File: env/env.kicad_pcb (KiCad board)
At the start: 2 copper layers, 69.1 x 99.6 mm, 35 parts, among them J1 Conn_01x02_Socket, J2 Conn_01x03_Socket, J3 Conn_01x02_Socket, J4 Conn_01x02_Socket, Q1 BC548C, SW1 SW_SPDT, U1 TL074, U2 TL074

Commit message: turn vca to dual vca add mounting holes
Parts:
- added H1: MountingHole, MountingHole:MountingHole_2.1mm, F.Cu at (166.1, 51.3)
- added H2: MountingHole, MountingHole:MountingHole_2.1mm, F.Cu at (107.7, 50.8)
- added H3: MountingHole, MountingHole:MountingHole_2.1mm, F.Cu at (164.1, 137.7)
- added H4: MountingHole, MountingHole:MountingHole_2.1mm, F.Cu at (110.2, 137.7)
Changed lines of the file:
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@@
   (net 28 "Net-(U2C--)")
   (net 29 "Net-(U2D--)")
+  (footprint "MountingHole:MountingHole_2.1mm" (layer "F.Cu")
+    (at 164.084 137.668)
+    (descr "Mounting Hole 2.1mm, no annular")
+    (tags "mounting hole 2.1mm no annular")
+    (property "Sheetfile" "env.kicad_sch")
+    (property "Sheetname" "")
+    (property "ki_description" "Mounting Hole without connection")
+    (property "ki_keywords" "mounting hole")
+    (attr exclude_from_pos_files)
+    (fp_text reference "H3" (at 0 -3.2) (layer "F.SilkS")
+        (effects (font (size 1 1) (thickness 0.15)))
+    )
+    (fp_text value "MountingHole" (at 0 3.2) (layer "F.Fab")
+        (effects (font (size 1 1) (thickness 0.15)))
+    )
+    (fp_text user "${REFERENCE}" (at 0 0) (layer "F.Fab")
+        (effects (font (size 1 1) (thickness 0.15)))
+    )
+    (fp_circle (center 0 0) (end 2.1 0)
+      (stroke (width 0.15) (type solid)) (fill none) (layer "Cmts.User"))
+    (fp_circle (center 0 0) (end 2.35 0)
+      (stroke (width 0.05) (type solid)) (fill none) (layer "F.CrtYd"))
+    (pad "" np_thru_hole circle (at 0 0) (size 2.1 2.1) (drill 2.1) (layers "*.Cu" "*.Mask"))
+  )
   (footprint "my_library:my_dip14" (layer "F.Cu")
     (at 132.1598 64.516)
@@
     )
   )
+  (footprint "MountingHole:MountingHole_2.1mm" (layer "F.Cu")
+    (at 110.236 137.668)
+    (descr "Mounting Hole 2.1mm, no annular")
+    (tags "mounting hole 2.1mm no annular")
+    (property "Sheetfile" "env.kicad_sch")
+    (property "Sheetname" "")
+    (property "ki_description" "Mounting Hole without connection")
+    (property "ki_keywords" "mounting hole")
+    (attr exclude_from_pos_files)
+    (fp_text reference "H4" (at 0 -3.2) (layer "F.SilkS")
+        (effects (font (size 1 1) (thickness 0.15)))
+    )
+    (fp_text value "MountingHole" (at 0 3.2) (layer "F.Fab")
+        (effects (font (size 1 1) (thickness 0.15)))
+    )
+    (fp_text user "${REFERENCE}" (at 0 0) (layer "F.Fab")
+        (effects (font (size 1 1) (thickness 0.15)))
+    )
+    (fp_circle (center 0 0) (end 2.1 0)
+      (stroke (width 0.15) (type solid)) (fill none) (layer "Cmts.User"))
+    (fp_circle (center 0 0) (end 2.35 0)
+      (stroke (width 0.05) (type solid)) (fill none) (layer "F.CrtYd"))
+    (pad "" np_thru_hole circle (at 0 0) (size 2.1 2.1) (drill 2.1) (layers "*.Cu" "*.Mask"))
+  )
   (footprint "my_library:my_really_cool_2pin" (layer "F.Cu")
     (at 161.1108 104.648)
@@
     (pad "3" thru_hole circle (at 0 7.62) (size 2.54 2.54) (drill 1) (layers "*.Cu" "*.Mask")
       (net 2 "GND") (pinfunction "3") (pintype "passive"))
+  )
+  (footprint "MountingHole:MountingHole_2.1mm" (layer "F.Cu")
+    (at 166.116 51.308)
+    (descr "Mounting Hole 2.1mm, no annular")
+    (tags "mounting hole 2.1mm no annular")
+    (property "Sheetfile" "env.kicad_sch")
+    (property "Sheetname" "")
+    (property "ki_description" "Mounting Hole without connection")
+    (property "ki_keywords" "mounting hole")
+    (attr exclude_from_pos_files)
+    (fp_text reference "H1" (at 0 -3.2) (layer "F.SilkS")
+        (effects (font (size 1 1) (thickness 0.15)))
+    )
+    (fp_text value "MountingHole" (at 0 3.2) (layer "F.Fab")
+        (effects (font (size 1 1) (thickness 0.15)))
+    )
+    (fp_text user "${REFERENCE}" (at 0 0) (layer "F.Fab")
+        (effects (font (size 1 1) (thickness 0.15)))
+    )
+    (fp_circle (center 0 0) (end 2.1 0)
+      (stroke (width 0.15) (type solid)) (fill none) (layer "Cmts.User"))
+    (fp_circle (center 0 0) (end 2.35 0)
+      (stroke (width 0.05) (type solid)) (fill none) (layer "F.CrtYd"))
+    (pad "" np_thru_hole circle (at 0 0) (size 2.1 2.1) (drill 2.1) (layers "*.Cu" "*.Mask"))
   )
   (footprint "my_library:my_really_cool_3pin" (layer "F.Cu")
@@
       (net 14 "Net-(D7-A)") (pintype "passive") (solder_mask_margin 0.102))
   )
+  (footprint "MountingHole:MountingHole_2.1mm" (layer "F.Cu")
+    (at 107.696 50.8)
+    (descr "Mounting Hole 2.1mm, no annular")
+    (tags "mounting hole 2.1mm no annular")
+    (property "Sheetfile" "env.kicad_sch")
+    (property "Sheetname" "")
+    (property "ki_description" "Mounting Hole without connection")
+    (property "ki_keywords" "mounting hole")
+    (attr exclude_from_pos_files)
+    (fp_text reference "H2" (at 0 -3.2) (layer "F.SilkS")
+        (effects (font (size 1 1) (thickness 0.15)))
+    )
+    (fp_text value "MountingHole" (at 0 3.2) (layer "F.Fab")
+        (effects (font (size 1 1) (thickness 0.15)))
+    )
+    (fp_text user "${REFERENCE}" (at 0 0) (layer "F.Fab")
+        (effects (font (size 1 1) (thickness 0.15)))
+    )
+    (fp_circle (center 0 0) (end 2.1 0)
+      (stroke (width 0.15) (type solid)) (fill none) (layer "Cmts.User"))
+    (fp_circle (center 0 0) (end 2.35 0)
+      (stroke (width 0.05) (type solid)) (fill none) (layer "F.CrtYd"))
+    (pad "" np_thru_hole circle (at 0 0) (size 2.1 2.1) (drill 2.1) (layers "*.Cu" "*.Mask"))
+  )
   (footprint "Resistor_THT:R_Axial_DIN0204_L3.6mm_D1.6mm_P7.62mm_Horizontal" (layer "F.Cu")

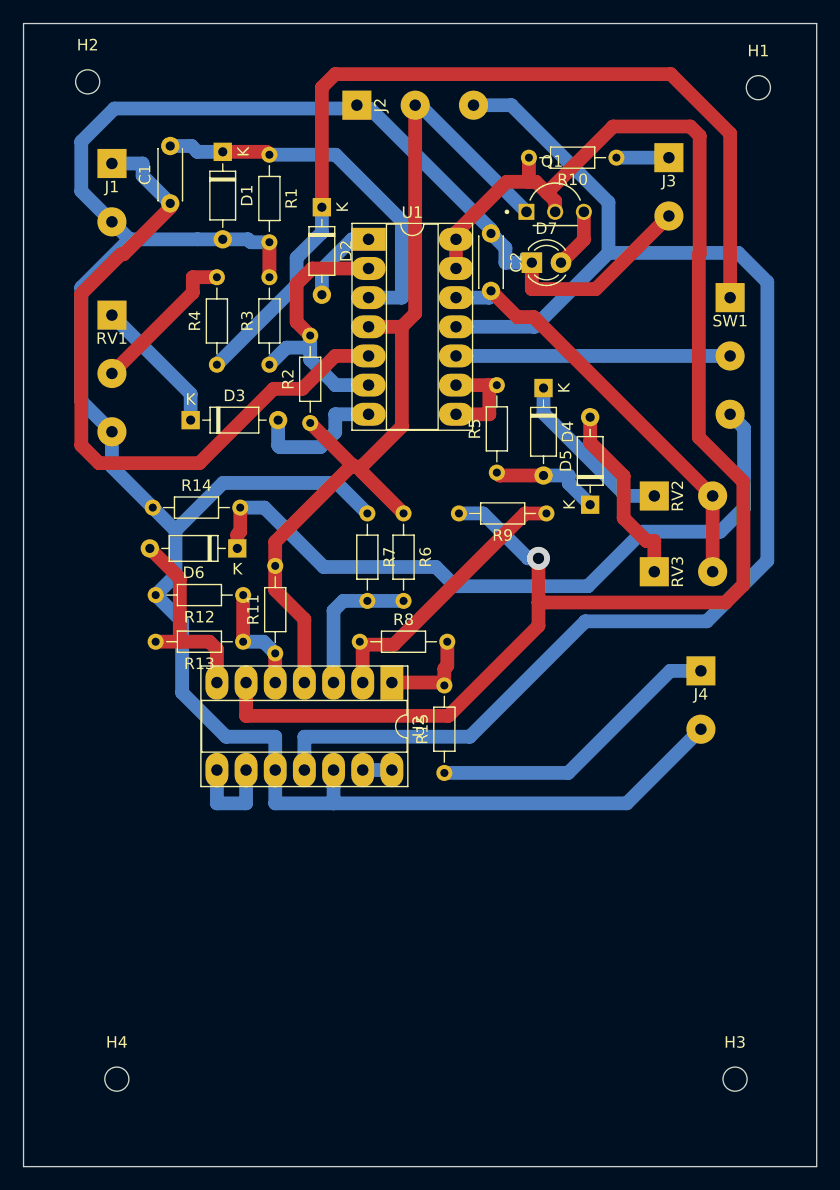
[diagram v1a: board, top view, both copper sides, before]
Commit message: use custom footprints with bigger pads
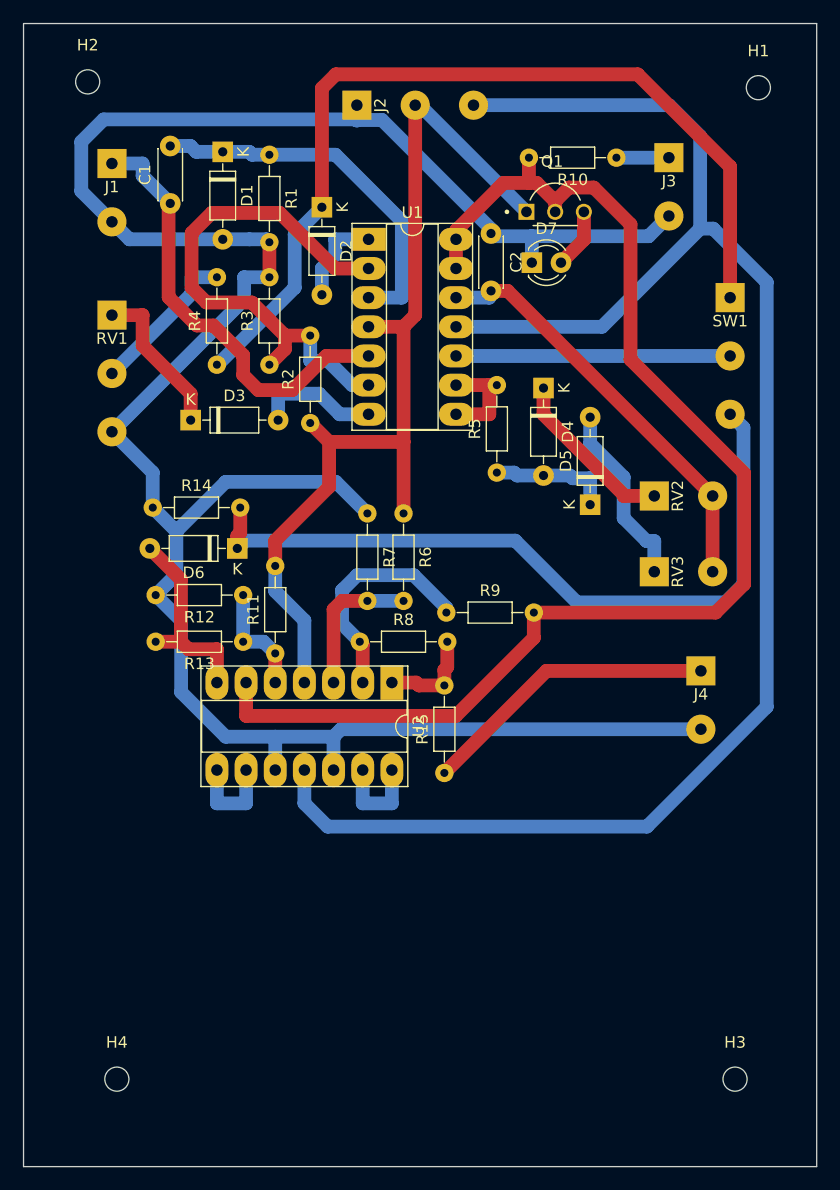
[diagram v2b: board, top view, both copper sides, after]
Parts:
- C1, C2: footprint Capacitor_THT:C_Disc_D4.3mm_W1.9mm_P5.00mm -> my_library:my_tht_cap
- D1, D2, D3, D4, D5, D6: footprint Diode_THT:D_DO-35_SOD27_P7.62mm_Horizontal -> my_library:my_tht_diode
- R1, R10, R11, R12, R13, R14, R15, R2, R3, R4, R5, R6, R7, R8, R9: footprint Resistor_THT:R_Axial_DIN0204_L3.6mm_D1.6mm_P7.62mm_Horizontal -> my_library:my_tht_r
- moved R9 12.3 mm to (138.9, 97.0), turned to 0 degrees
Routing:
- net Net-(U1D--): track 138.7 -> 113.6 mm, vias 1 -> 0
- net Net-(J1-Pin_1): track 61.1 -> 38.4 mm
- net -12V: track 124.4 -> 146.8 mm
- net Net-(U1A--): track 24.1 -> 46.2 mm
- net GND: track 213.7 -> 206.0 mm
- net Net-(U2D--): track 2.54 -> 8.34 mm
- net Net-(U2A--): track 24.4 -> 20.0 mm
- net Net-(D6-K): track 61.9 -> 66.2 mm
- net Net-(D2-K): track 80.4 -> 78.7 mm
- net Net-(D3-K): track 12.0 -> 13.5 mm
- net Net-(D3-A): track 12.2 -> 10.9 mm
- net +12V: track 84.3 -> 85.3 mm
- net Net-(D4-A): track 9.68 -> 10.6 mm
- net Net-(D2-A): track 7.35 -> 8.21 mm

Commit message: FRIENDSHIP ENDED WITH PACKAGE_DIP. added a keep-out on F.cu for dip14
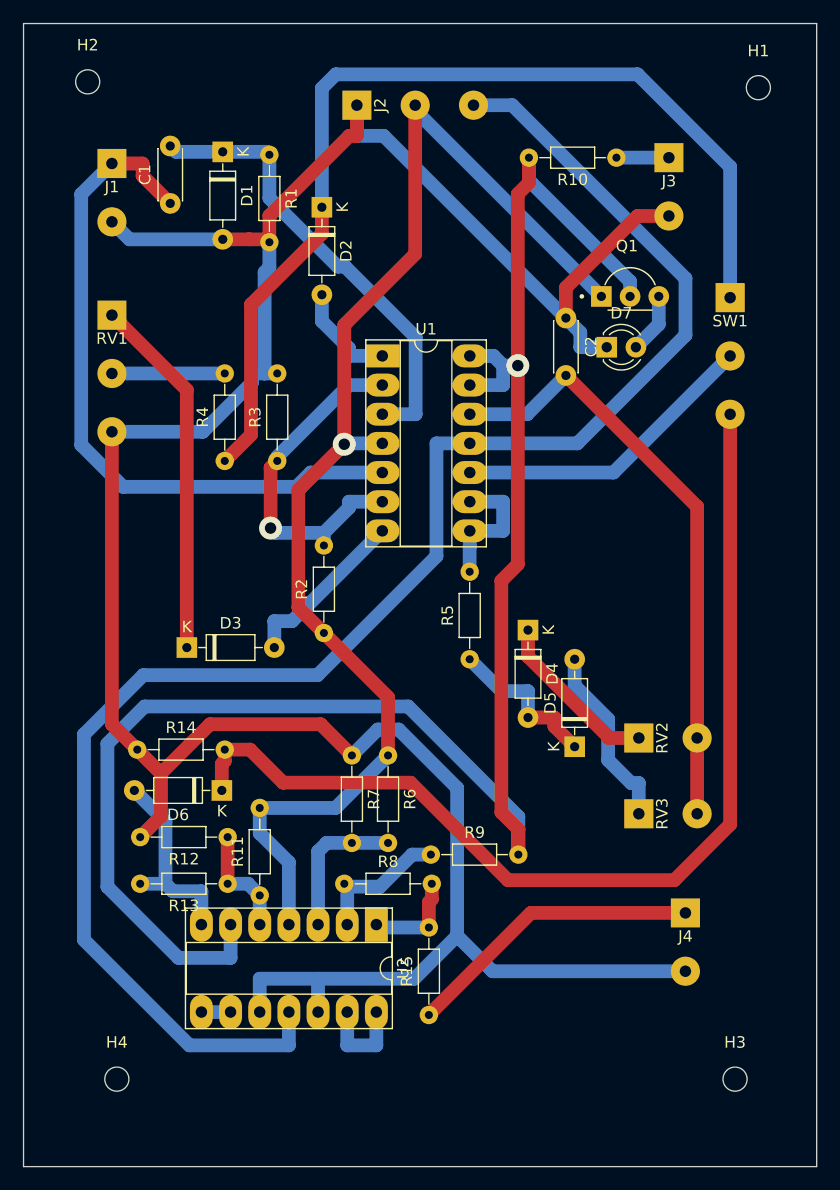
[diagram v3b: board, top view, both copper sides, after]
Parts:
- Q1: footprint BC548C:TO92250P510H770-3 -> my_library:my_bc548
- U1, U2: footprint my_library:my_dip14 -> my_library:my_dip14_no_f_pads
- moved D6 21.1 mm to (119.4, 112.5)
- moved J4 21.1 mm to (159.8, 125.7)
- moved R15 21.1 mm to (137.4, 132.1)
- moved RV2 21.1 mm to (158.2, 108.0)
- moved RV3 21.1 mm to (158.2, 114.6)
- moved D4 21.1 mm to (146.1, 98.6)
- moved D5 21.1 mm to (150.1, 108.7)
- moved R13 21.1 mm to (119.9, 120.7)
- moved R6 21.1 mm to (133.9, 109.5)
- moved R7 21.1 mm to (130.7, 109.5)
- moved R8 21.1 mm to (130.0, 120.7)
- moved U2 21.1 mm to (132.8, 124.2)
- moved R11 21.1 mm to (122.7, 121.7)
- moved R14 21.1 mm to (112.0, 109.0)
- moved R12 21.1 mm to (119.9, 116.6)
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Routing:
- net Net-(U1D--): track 113.6 -> 160.4 mm, vias 0 -> 1
- net +12V: track 85.3 -> 115.1 mm, vias 0 -> 1
- net GND: track 206.0 -> 233.6 mm
- net Net-(D6-K): track 66.2 -> 90.1 mm
- net Net-(J1-Pin_1): track 38.4 -> 61.0 mm
- net Net-(D3-K): track 13.5 -> 31.7 mm
- net Net-(U1D-+): track 36.9 -> 52.7 mm
- net Net-(U1A--): track 46.2 -> 30.6 mm, vias 0 -> 1
- net Net-(D2-K): track 78.7 -> 86.8 mm
- net Net-(U2A--): track 20.0 -> 12.1 mm
- net Net-(D1-K): track 32.5 -> 40.1 mm
- net Net-(U2C--): track 8.34 -> 2.54 mm
- net Net-(D3-A): track 10.9 -> 15.0 mm
- net Net-(R4-Pad2): track 13.5 -> 9.83 mm
- net Net-(D4-A): track 10.6 -> 14.1 mm
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
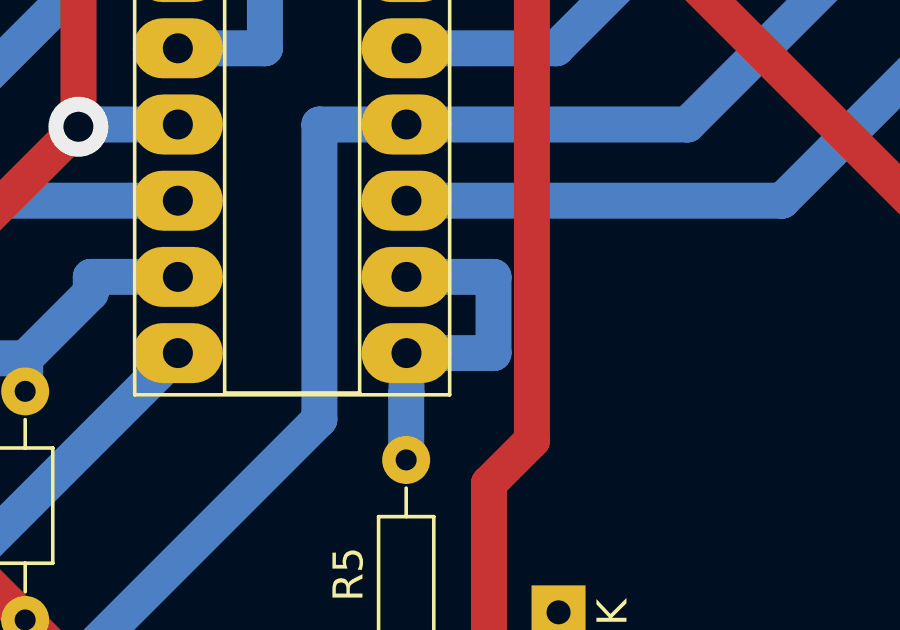
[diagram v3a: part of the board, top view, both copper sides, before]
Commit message: some notes about front panel construction and some boms
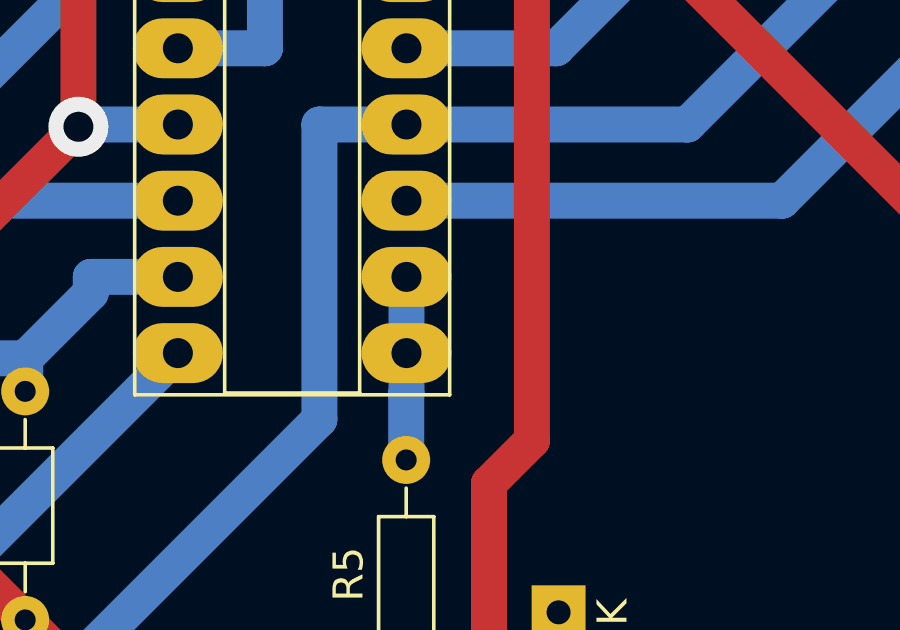
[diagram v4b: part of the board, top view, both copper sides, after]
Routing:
- net Net-(U1C--): track 11.9 -> 6.11 mm
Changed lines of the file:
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@@
   (segment (start 140.97 93.472) (end 140.97 91.2701) (width 1.2) (layer "B.Cu") (net 22))
   (segment (start 140.98 91.2601) (end 140.98 89.911) (width 1.2) (layer "B.Cu") (net 22))
-  (segment (start 140.98 87.371) (end 143.8819 87.371) (width 1.2) (layer "B.Cu") (net 22))
-  (segment (start 143.8819 89.911) (end 143.8819 87.371) (width 1.2) (layer "B.Cu") (net 22))
   (segment (start 140.97 91.2701) (end 140.98 91.2601) (width 1.2) (layer "B.Cu") (net 22))
-  (segment (start 140.98 89.911) (end 143.8819 89.911) (width 1.2) (layer "B.Cu") (net 22))
+  (segment (start 140.98 87.371) (end 140.98 89.911) (width 1.2) (layer "B.Cu") (net 22))
   (segment (start 127.762 117.8381) (end 127.762 124.206) (width 1.2) (layer "B.Cu") (net 23))
   (segment (start 133.858 117.094) (end 130.708 117.094) (width 1.2) (layer "B.Cu") (net 23))
